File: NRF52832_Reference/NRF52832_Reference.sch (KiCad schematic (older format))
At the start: 24 parts, among them J1 MM8130-2600RA2, U1 NRF52810-QFAA, Y1 32MHz, Y2 32.768kHz

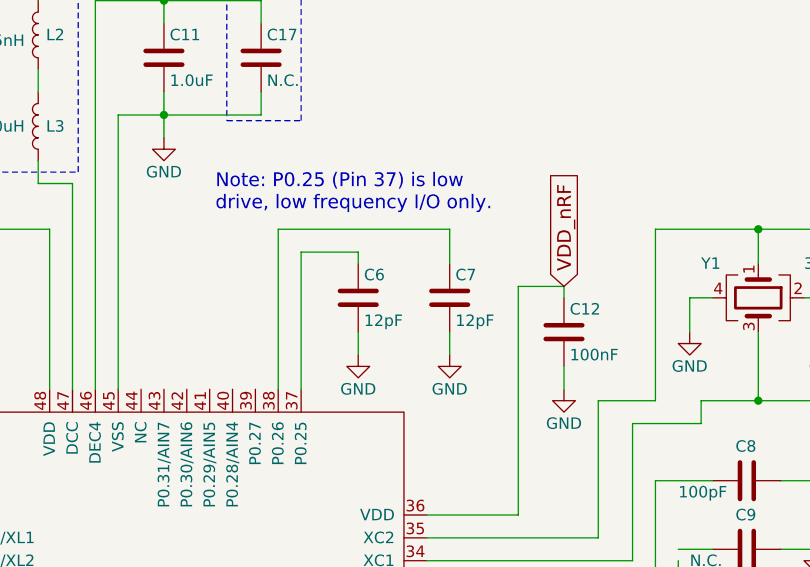
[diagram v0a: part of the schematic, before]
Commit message: Removed unneeded capacitors from P0.25 and P0.26
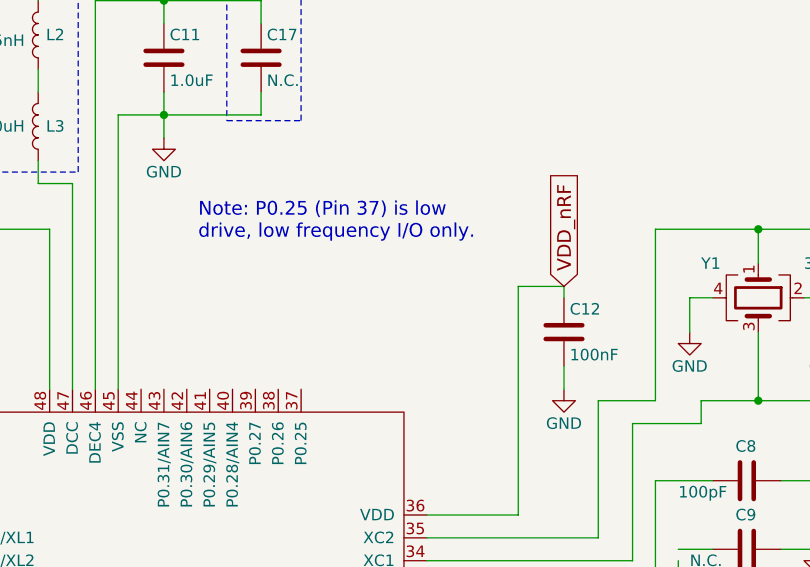
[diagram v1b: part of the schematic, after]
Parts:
- removed C6, C7: 12pF, Capacitors_SMD:C_0402, symbol Device:C
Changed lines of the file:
@@
-$EndComp
-$Comp
-L Device:C C6
-U 1 1 5B5B72F5
-P 6200 2850
-F 0 "C6" H 6225 2950 50  0000 L CNN
-F 1 "12pF" H 6225 2750 50  0000 L CNN
-F 2 "Capacitors_SMD:C_0402" H 6238 2700 50  0001 C CNN
-F 3 "" H 6200 2850 50  0001 C CNN
-	1    6200 2850
-	1    0    0    -1
-$EndComp
-$Comp
-L Device:C C7
-U 1 1 5B5B7383
-P 6600 2850
-F 0 "C7" H 6625 2950 50  0000 L CNN
-F 1 "12pF" H 6625 2750 50  0000 L CNN
-F 2 "Capacitors_SMD:C_0402" H 6638 2700 50  0001 C CNN
-F 3 "" H 6600 2850 50  0001 C CNN
-	1    6600 2850
-	1    0    0    -1
 $EndComp
 $Comp
@@
 	1    7900 3650
 	0    1    1    0
-$EndComp
-$Comp
-L power:GND #PWR02
-U 1 1 5B5B7E31
-P 6200 3100
-F 0 "#PWR02" H 6200 2850 50  0001 C CNN
-F 1 "GND" H 6200 2950 50  0000 C CNN
-F 2 "" H 6200 3100 50  0001 C CNN
-F 3 "" H 6200 3100 50  0001 C CNN
-	1    6200 3100
-	1    0    0    -1
-$EndComp
-$Comp
-L power:GND #PWR03
-U 1 1 5B5B7E69
-P 6600 3100
-F 0 "#PWR03" H 6600 2850 50  0001 C CNN
-F 1 "GND" H 6600 2950 50  0000 C CNN
-F 2 "" H 6600 3100 50  0001 C CNN
-F 3 "" H 6600 3100 50  0001 C CNN
-	1    6600 3100
-	1    0    0    -1
 $EndComp
 $Comp
@@
 	7750 3650 7500 3650
 Wire Wire Line
-	5950 3250 5950 2650
-Wire Wire Line
-	5950 2650 6200 2650
-Wire Wire Line
-	6200 2650 6200 2700
-Wire Wire Line
-	5850 3250 5850 2550
-Wire Wire Line
-	5850 2550 6600 2550
-Wire Wire Line
-	6600 2550 6600 2700
-Wire Wire Line
-	6200 3100 6200 3000
-Wire Wire Line
-	6600 3100 6600 3000
-Wire Wire Line
 	4850 2550 4850 3250
 Wire Wire Line
@@
 Wire Notes Line
 	5950 2075 5950 1350
-Text Notes 5575 2475 0    60   ~ 0
+Text Notes 5500 2600 0    60   ~ 0
 Note: P0.25 (Pin 37) is low\ndrive, low frequency I/O only.
 Wire Wire Line

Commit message: Added power circuit for NRF52. Added SMT Practice V1 project. Modified Motor v2 project.
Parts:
- removed C1: 0.8pF, Capacitors_SMD:C_0402, symbol Device:C
- removed C10: 1.2pF, Capacitors_SMD:C_0402, symbol Device:C
- removed C11: 1.0uF, Capacitors_SMD:C_0603, symbol Device:C
- removed C12, C2, C5: 100nF, Capacitors_SMD:C_0402, symbol Device:C
- removed C13, C15, C16: 12pF, Capacitors_SMD:C_0402, symbol Device:C
- removed C14: 12nF, Capacitors_SMD:C_0402, symbol Device:C
- removed C17, C3, C9: N.C., Capacitors_SMD:C_0402, symbol Device:C
- removed C4: 4.7uF, Capacitors_SMD:C_0603, symbol Device:C
- removed C8: 100pF, Capacitors_SMD:C_0402, symbol Device:C
- removed J1: MM8130-2600RA2, MM8130-2600RA2:MURATA_MM8130-2600RA2, symbol MM8130-2600RA2:MM8130-2600RA2
- removed L1: 3.9nH, Inductors_SMD:L_0402, symbol Device:L
- removed L2: 15nH, Inductors_SMD:L_0402, symbol Device:L
- removed L3: 10uH, Inductors_SMD:L_0603, symbol Device:L
- removed U1: NRF52810-QFAA, Package_DFN_QFN:QFN-48-1EP_6x6mm_P0.4mm_EP4.66x4.66mm_ThermalVias, symbol Project_Libary:nRF52832
- removed Y1: 32MHz, Crystals:Crystal_SMD_2016-4pin_2.0x1.6mm, symbol Device:Crystal_GND24
- removed Y2: 32.768kHz, Crystals:Crystal_SMD_3215-2pin_3.2x1.5mm, symbol Device:Crystal
- added D?: LED, symbol Device:LED
- added J? (x3): Conn_01x10_Male, symbol Connector:Conn_01x10_Male
- added J?: Conn_01x02_Male, symbol Connector:Conn_01x02_Male
- added J?: Conn_ARM_JTAG_SWD_10, Connector_PinHeader_1.27mm:PinHeader_2x05_P1.27mm_Vertical_SMD, symbol Connector:Conn_ARM_JTAG_SWD_10
- added R?: R_PHOTO, symbol Device:R_PHOTO
- added R?: R, symbol Device:R
- added U?: DA56-11YWA, Display_7Segment:DA56-11SYKWA, symbol Display_Character:DA56-11YWA
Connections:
- net labels added: 3V3_Ref, 5V_Ref
- net labels removed: ANT, RF, VDD_nRF
- wire segments 98 -> 8
- no-connect marks 2 -> 0
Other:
- note added: "Photoresistor w/\njumper pins"
- note added: "Power Supply"
- note added: "Power\nLED"
- note added: "SWD Interface"
- note removed: "Note: Make sure the antenna is at least 5mm away from the ground plane.\nThis also applies to the layers below the antenna. For best reliability,\nthe side of the PCB with the antenna should be the closest to the edge of\nthe housing."
- note removed: "Note: P0.25 (Pin 37) is low\ndrive, low frequency I/O only."
- note removed: "Optional: External 32kHz clock is more efficient\nand accurate than the internal RC oscillator"
- note removed: "Optional: For DC/DC regulator"

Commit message: Added I2C components: 4KB EEPROM, Light sensor, and Temp sensor to schematic.
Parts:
- removed J?: Conn_01x02_Male, symbol Connector:Conn_01x02_Male
- removed R?: R_PHOTO, symbol Device:R_PHOTO
- removed U?: DA56-11YWA, Display_7Segment:DA56-11SYKWA, symbol Display_Character:DA56-11YWA
- added C? (x3): 0.1uF, symbol Device:C
- added J? (x2): Conn_01x02_Male, symbol Connector:Conn_01x02_Male
- added R? (x2): 10k, symbol Device:R
- added U?: AT34C04-X5M-T, symbol Project_Libary:AT34C04-X5M-T
- added U?: LTR-329ALS-01, symbol Project_Libary:LTR-329ALS-01
- added U?: TCN75AVUA713, symbol Project_Libary:TCN75AVUA713
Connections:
- net labels added: P0.11_SDA, P0.12_SCL
- wire segments 8 -> 63
- no-connect marks 0 -> 1
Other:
- note added: "EEPROM 4KB"
- note added: "I2C Bus Components w/ jumpers to disconnect the bus to free I/O if needed"
- note added: "Light Sensor"
- note added: "Power"
- note added: "Temp Sensor"
- note removed: "Photoresistor w/\njumper pins"
- note removed: "Power Supply"
- moved on the sheet: D?, J?, R?

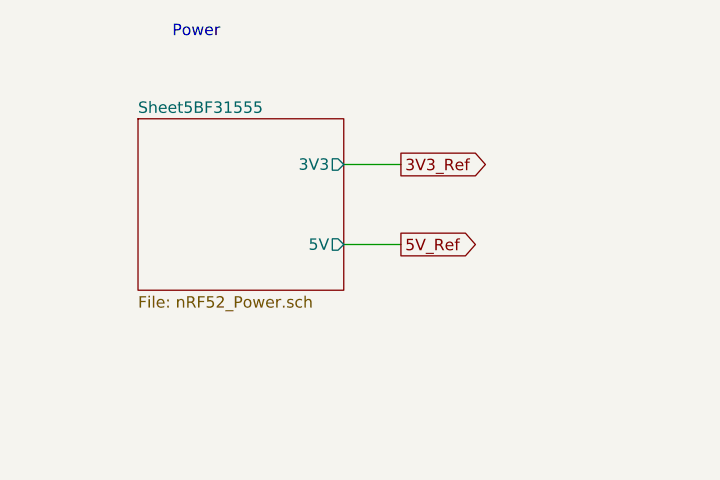
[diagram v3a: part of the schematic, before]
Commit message: Updated Boost conv. components and moved 3.3V regulator.
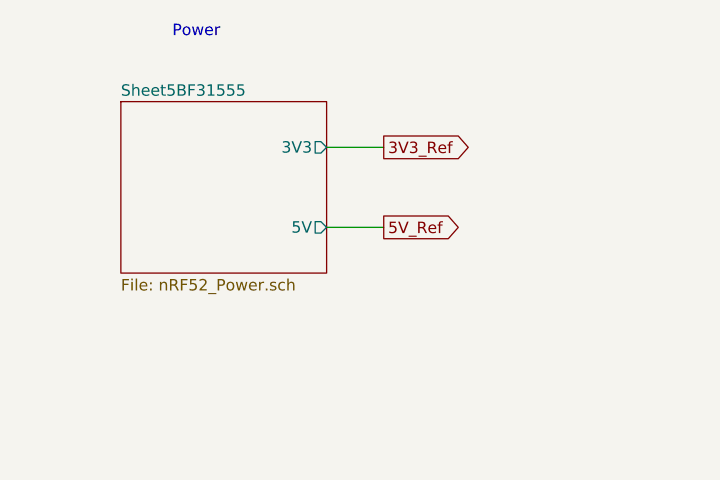
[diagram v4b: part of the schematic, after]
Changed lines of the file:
@@
 SWD Interface
 $Sheet
-S 1000 1100 900  750
+S 925  1025 900  750
 U 5BF31556
 F0 "Sheet5BF31555" 50
 F1 "nRF52_Power.sch" 50
-F2 "3V3" O R 1900 1300 50
-F3 "5V" O R 1900 1650 50
+F2 "3V3" O R 1825 1225 50
+F3 "5V" O R 1825 1575 50
 $EndSheet
 Text Notes 1150 750  0    50   ~ 0
@@
 	10100 6000 10100 6100
 Wire Wire Line
-	1900 1300 2150 1300
+	1825 1225 2075 1225
 Wire Wire Line
-	1900 1650 2150 1650
-Text GLabel 2150 1300 2    50   Output ~ 0
+	1825 1575 2075 1575
+Text GLabel 2075 1225 2    50   Output ~ 0
 3V3_Ref
-Text GLabel 2150 1650 2    50   Output ~ 0
+Text GLabel 2075 1575 2    50   Output ~ 0
 5V_Ref
 Text GLabel 10400 5300 2    50   Input ~ 0

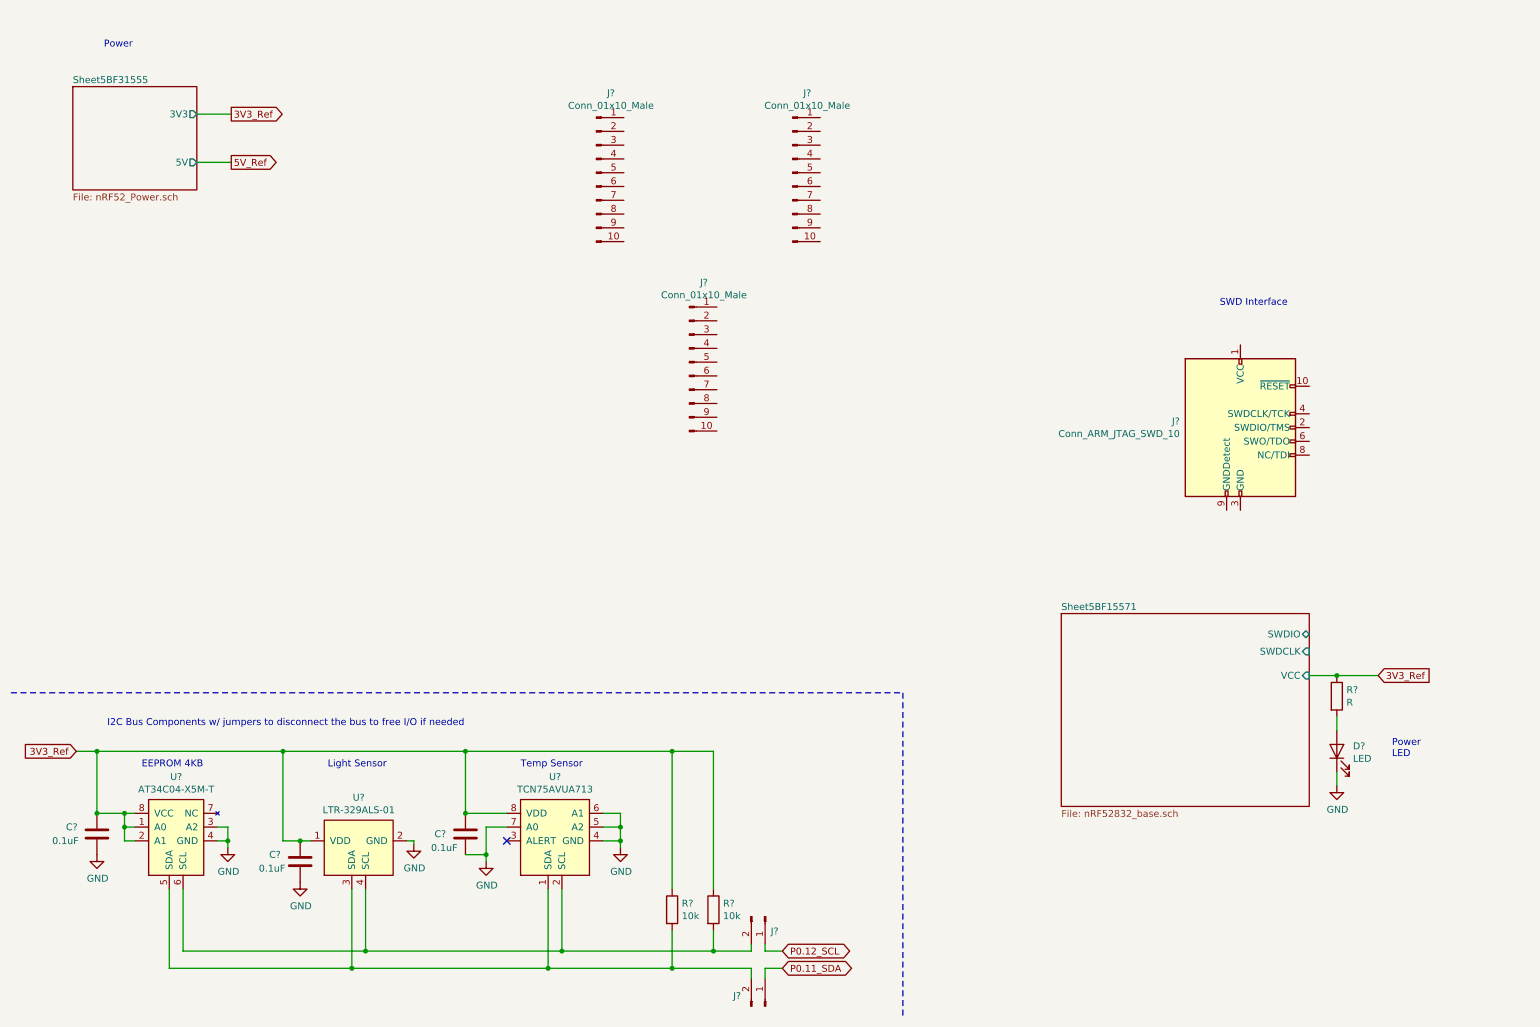
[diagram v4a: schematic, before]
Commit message: Updated SWD interface headers
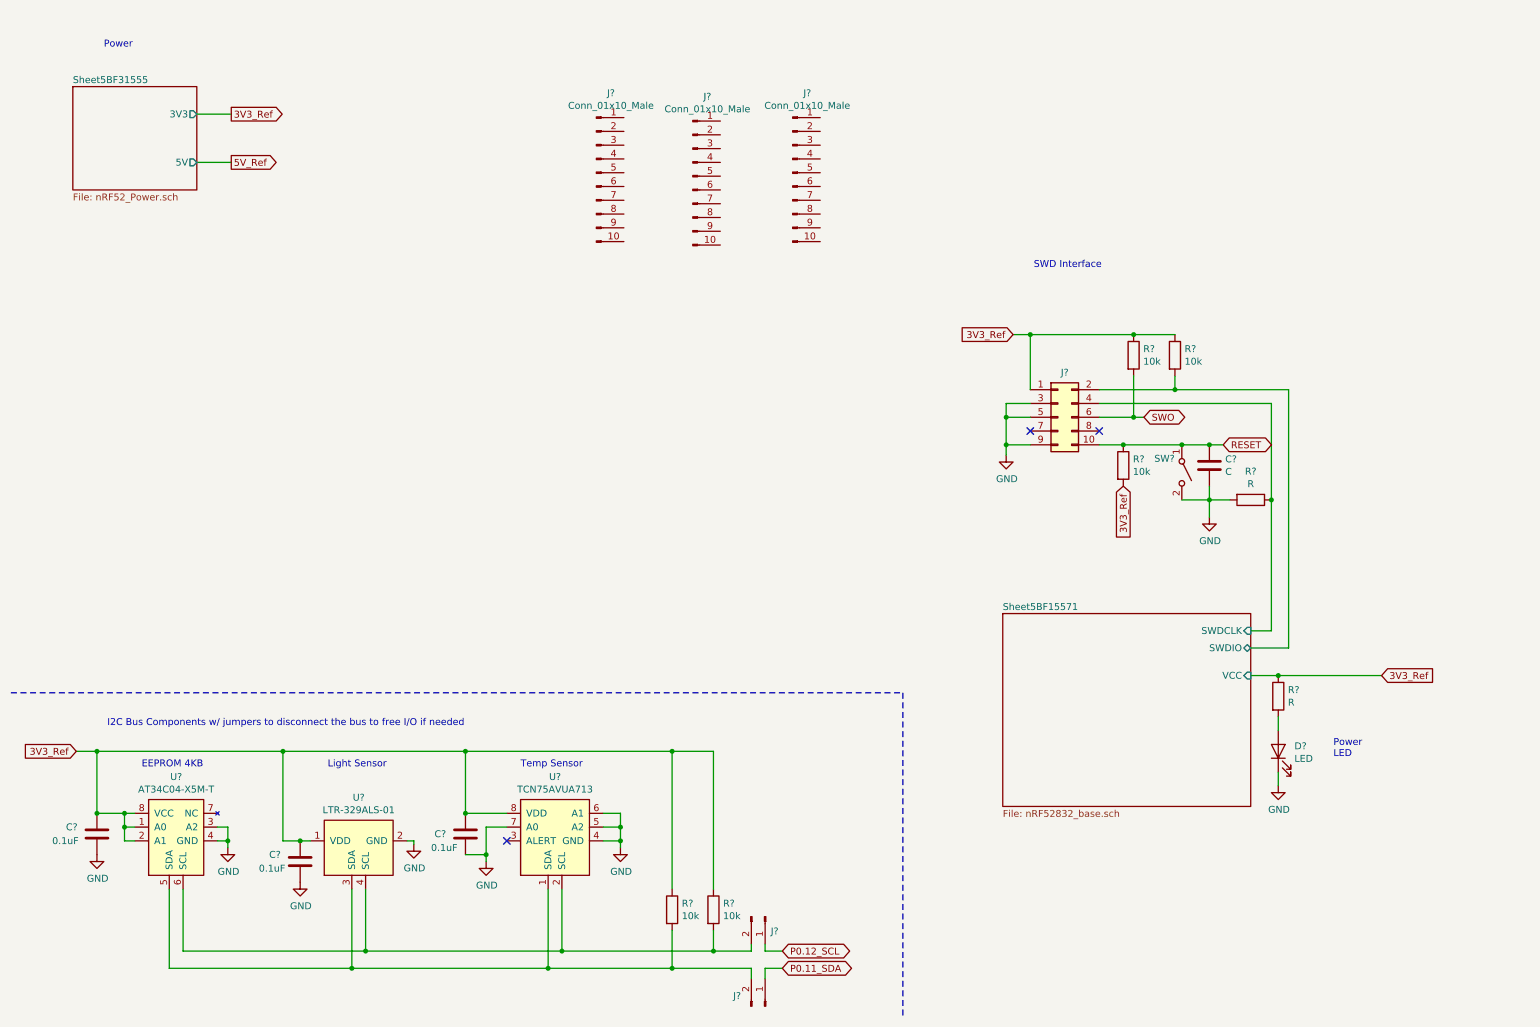
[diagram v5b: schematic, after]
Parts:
- removed J?: Conn_ARM_JTAG_SWD_10, Connector_PinHeader_1.27mm:PinHeader_2x05_P1.27mm_Vertical_SMD, symbol Connector:Conn_ARM_JTAG_SWD_10
- added C?: C, symbol Device:C
- added J?: Conn_02x05_Odd_Even, symbol Connector_Generic:Conn_02x05_Odd_Even
- added R? (x3): 10k, symbol Device:R
- added R?: R, symbol Device:R
- added SW?: SW_SPST, symbol Switch:SW_SPST
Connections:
- net 3V3_Ref: now also J?.1 (Pin_1), R?.1, R?.1, R?.2
- net GND: now also C?.2, J?.3 (Pin_3), J?.5 (Pin_5), J?.9 (Pin_9), R?.2, SW?.2 (B)
- net Sheet5BF15571/SWDCLK: now also J?.4 (Pin_4), R?.1
- net Sheet5BF15571/SWDIO: now also J?.2 (Pin_2), R?.2
- new net RESET: C?.1, J?.10 (Pin_10), R?.1, SW?.1 (A)
- new net SWO: J?.6 (Pin_6), R?.2
- no-connect marks 1 -> 3
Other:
- moved on the sheet: D?, J?, R?
